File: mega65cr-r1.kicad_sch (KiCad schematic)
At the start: 0 parts

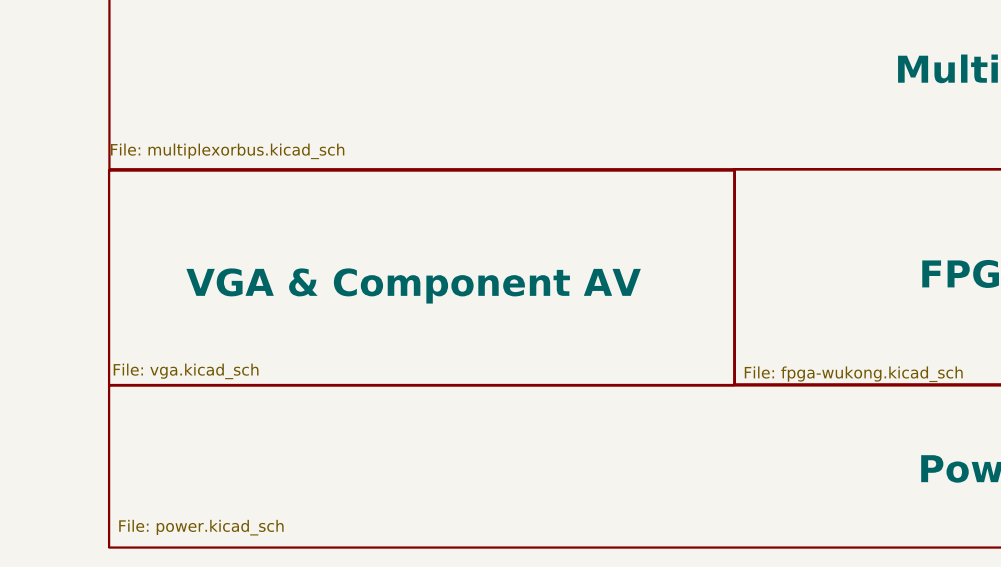
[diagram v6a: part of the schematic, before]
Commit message: add C64 keyboard connector on MUX bus #9
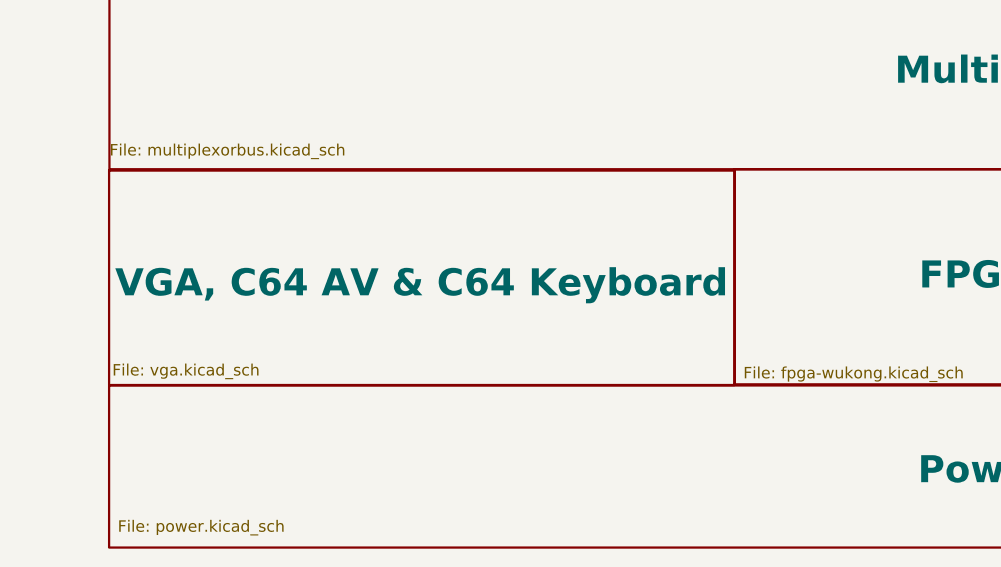
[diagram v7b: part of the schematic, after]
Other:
- sheet VGA & Component AV renamed VGA, C64 AV & C64 Keyboard
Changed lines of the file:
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@@
     (stroke (width 0.25) (type solid) (color 0 0 0 0))
     (fill (color 255 208 70 1.0000))
-    (property "Sheet name" "VGA & Component AV" (id 0) (at 34.5694 127.6985 0)
+    (property "Sheet name" "VGA, C64 AV & C64 Keyboard" (id 0) (at 26.67 127.635 0)
       (effects (font (size 3 3) bold) (justify left bottom))
     )
@@
       (reference "#PWR0293") (unit 1) (value "GND") (footprint "")
     )
+    (path "/3e79ecec-be2d-46e5-9b86-3d84ade3f323/05212271-1bdb-4db0-a1bd-f6bdd2f3ddec"
+      (reference "#PWR?") (unit 1) (value "+3.3V") (footprint "")
+    )
     (path "/46f1890f-c5bb-4aae-8808-0511f47e29d8/230614ab-5f6d-4eb9-9b18-b4ff984cf93b"
       (reference "#PWR?") (unit 1) (value "GND") (footprint "")
@@
       (reference "#PWR?") (unit 1) (value "+3.3V") (footprint "")
     )
+    (path "/3e79ecec-be2d-46e5-9b86-3d84ade3f323/530b35e5-e228-472e-a735-6496fc19b354"
+      (reference "#PWR?") (unit 1) (value "GND") (footprint "")
+    )
+    (path "/3e79ecec-be2d-46e5-9b86-3d84ade3f323/57923e41-00a7-4666-8f26-e80e4c2fdc90"
+      (reference "#PWR?") (unit 1) (value "GND") (footprint "")
+    )
+    (path "/3e79ecec-be2d-46e5-9b86-3d84ade3f323/7584ad60-fa29-4a20-8bf9-ec3c0ac88099"
+      (reference "#PWR?") (unit 1) (value "+5V") (footprint "")
+    )
+    (path "/3e79ecec-be2d-46e5-9b86-3d84ade3f323/80f38011-f89d-40e1-b90a-06ae01572e7c"
+      (reference "#PWR?") (unit 1) (value "+5V") (footprint "")
+    )
     (path "/46f1890f-c5bb-4aae-8808-0511f47e29d8/8cc23d8d-40d1-4643-aada-b1561120c39b"
       (reference "#PWR?") (unit 1) (value "+3.3V") (footprint "")
     )
+    (path "/3e79ecec-be2d-46e5-9b86-3d84ade3f323/98e1dc96-efa7-43a7-8ef3-6339b9a020bf"
+      (reference "#PWR?") (unit 1) (value "GND") (footprint "")
+    )
+    (path "/3e79ecec-be2d-46e5-9b86-3d84ade3f323/a2f80ac3-fef8-44a9-9acb-e67ec2e85af6"
+      (reference "#PWR?") (unit 1) (value "GND") (footprint "")
+    )
     (path "/46f1890f-c5bb-4aae-8808-0511f47e29d8/c26c6650-b859-4f64-a618-5ffc5e31b556"
       (reference "#PWR?") (unit 1) (value "GND") (footprint "")
@@
     )
     (path "/3e79ecec-be2d-46e5-9b86-3d84ade3f323/f21fe63a-5618-45ac-a995-fde1476d25ed"
-      (reference "J23") (unit 1) (value "3.5mm_Stereo_Audio_Jack STX-3500-4N") (footprint "Connector_Audio:Jack_3.5mm_CUI_SJ-3524-SMT_Horizontal")
+      (reference "J23") (unit 1) (value "Audio Out") (footprint "Connector_Audio:Jack_3.5mm_CUI_SJ-3524-SMT_Horizontal")
     )
     (path "/3e79ecec-be2d-46e5-9b86-3d84ade3f323/808553aa-d67d-40d6-a901-9ceff4abc198"
@@
       (reference "J?") (unit 1) (value "Keyboard JTAG header") (footprint "Connector_PinHeader_2.54mm:PinHeader_2x05_P2.54mm_Vertical")
     )
+    (path "/3e79ecec-be2d-46e5-9b86-3d84ade3f323/2e2f9512-0b51-43d5-acc3-ec4f4b74c7e2"
+      (reference "J?") (unit 1) (value "Conn_01x20") (footprint "")
+    )
     (path "/46f1890f-c5bb-4aae-8808-0511f47e29d8/3a411649-1000-4244-bdff-03e5a7b1c1f8"
       (reference "J?") (unit 1) (value "MEGA65 Keyboard") (footprint "")
@@
       (reference "U42") (unit 7) (value "74LS06") (footprint "")
     )
+    (path "/3e79ecec-be2d-46e5-9b86-3d84ade3f323/dd334ca1-0e2a-4c9c-af75-615f814a7c65"
+      (reference "U?") (unit 1) (value "74LVC374") (footprint "Package_DIP:DIP-20_W7.62mm")
+    )
+    (path "/3e79ecec-be2d-46e5-9b86-3d84ade3f323/e5284eb9-4387-4bc4-9506-4c7f6ea4816d"
+      (reference "U?") (unit 1) (value "74LS374") (footprint "Package_DIP:DIP-20_W7.62mm")
+    )
   )

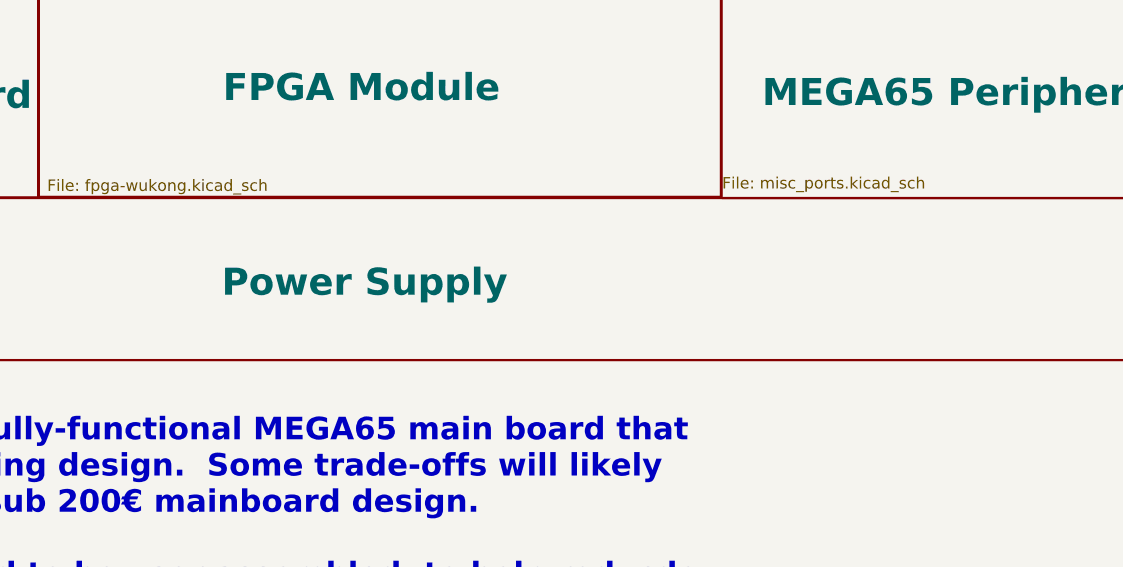
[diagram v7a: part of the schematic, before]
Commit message: place some mounting holes and reset button #3
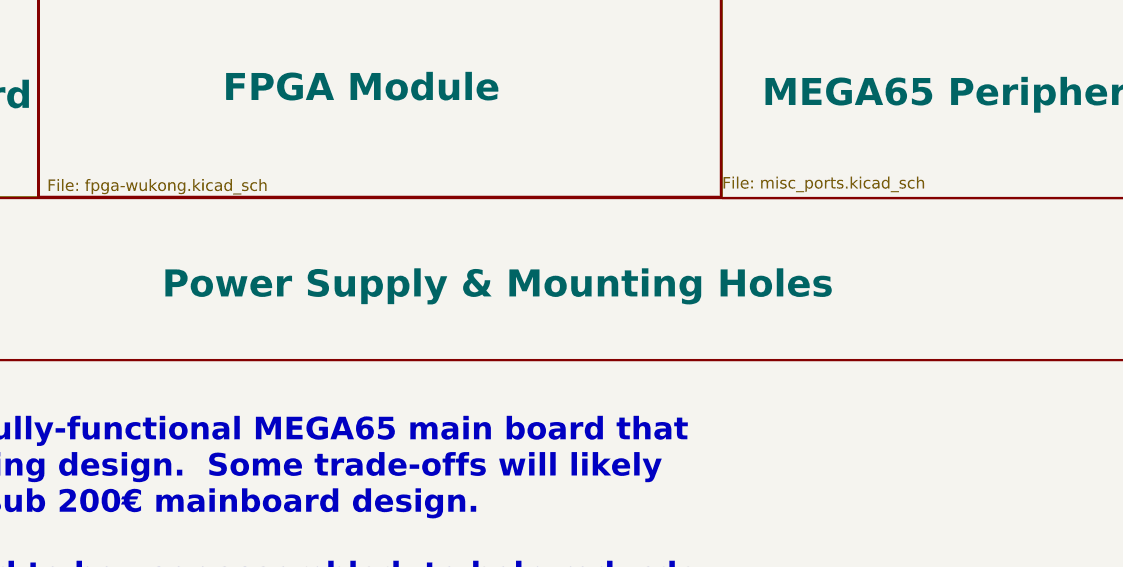
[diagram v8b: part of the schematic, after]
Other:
- sheet Power Supply renamed Power Supply & Mounting Holes
